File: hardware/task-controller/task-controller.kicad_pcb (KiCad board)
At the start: 2 copper layers, 64 parts, among them J1 USB_C_Receptacle_USB2.0_16P, SW1 User, SW2 RST, SW3 BOOTSEL, U1 RP2040, U2 TPS61023DRL, U3 FM24C64B, U4 W25Q32JVSS, U5 XC6206PxxxMR, Y1 12MHz

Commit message: started layout
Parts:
- removed BT1: Conn_01x02, Connector_JST:JST_PH_S2B-PH-SM4-TB_1x02-1MP_P2.00mm_Horizontal
- removed the C20 at (120.8, 67.9)
- removed the C21 at (120.8, 70.9)
- removed C3, C4, C5: 10uF, Capacitor_SMD:C_0805_2012Metric
- removed the D1 at (106.7, 83.2)
- removed D2: SS24, Diode_SMD:D_SMA
- removed F1: Polyfuse, Fuse:Fuse_1206_3216Metric
- removed JP1: ISENSE, Jumper:SolderJumper-2_P1.3mm_Bridged2Bar_RoundedPad1.0x1.5mm
- removed JP2: SolderJumper_2_Bridged, Jumper:SolderJumper-2_P1.3mm_Bridged2Bar_RoundedPad1.0x1.5mm
- removed JP3: Power_Bypass, Jumper:SolderJumper-2_P1.3mm_Bridged2Bar_RoundedPad1.0x1.5mm
- removed L1: 2.7uH, cat:Inductor_0806
- removed the R1 at (82.2, 79.9)
- removed the R4 at (82.2, 84.9)
- removed TP1, TP2: TestPoint, TestPoint:TestPoint_Pad_3.0x3.0mm
- removed the U5 at (166.9, 60.4)
- added C1: 1uF, Capacitor_SMD:C_0805_2012Metric, F.Cu at (33.6, 69.9)
- added C23: 1uF, Capacitor_SMD:C_0805_2012Metric, F.Cu at (18.5, 90.4)
- added C8: 1uF, Capacitor_SMD:C_0805_2012Metric, F.Cu at (33.6, 72.9)
- added J2: RGB 1, Connector_JST:JST_PH_B3B-PH-SM4-TB_1x03-1MP_P2.00mm_Vertical, F.Cu at (202.6, 87.2)
- added J3: RGB 2, Connector_JST:JST_PH_B3B-PH-SM4-TB_1x03-1MP_P2.00mm_Vertical, F.Cu at (202.6, 98.5)
- added J4: RGB 3, Connector_JST:JST_PH_B3B-PH-SM4-TB_1x03-1MP_P2.00mm_Vertical, F.Cu at (202.6, 109.8)
- added J5: Micro_SD_Card, Connector_Card:microSD_HC_Hirose_DM3AT-SF-PEJM5, F.Cu at (137.6, 84.3)
- added J6: Conn_01x06, Connector_PinHeader_2.54mm:PinHeader_1x06_P2.54mm_Vertical, F.Cu at (29.0, 70.7)
- added R23: 5.1k, Resistor_SMD:R_0402_1005Metric, F.Cu at (91.3, 16.8)
- added R24: 10k, Resistor_SMD:R_0402_1005Metric, F.Cu at (74.1, 0.49)
- added R25: 10k, Resistor_SMD:R_0402_1005Metric, F.Cu at (74.1, 2.48)
- added R26: 10k, Resistor_SMD:R_0402_1005Metric, F.Cu at (74.1, 4.47)
- added R27: 10k, Resistor_SMD:R_0402_1005Metric, F.Cu at (74.1, 6.46)
- added R28: 10k, Resistor_SMD:R_0402_1005Metric, F.Cu at (74.1, 8.46)
- added R29: 10k, Resistor_SMD:R_0402_1005Metric, F.Cu at (74.1, 10.4)
- added R30: 10k, Resistor_SMD:R_0402_1005Metric, F.Cu at (74.1, 12.4)
- added R31: 1k, Resistor_SMD:R_0402_1005Metric, F.Cu at (17.7, 69.3)
- added R32: 5.1k, Resistor_SMD:R_0402_1005Metric, F.Cu at (17.7, 71.3)
- added R33: 5.1k, Resistor_SMD:R_0402_1005Metric, F.Cu at (17.7, 73.3)
- added R34: 5.1k, Resistor_SMD:R_0402_1005Metric, F.Cu at (17.7, 75.3)
- added R35: 5.1k, Resistor_SMD:R_0402_1005Metric, F.Cu at (17.7, 77.3)
- added R36: 5.1k, Resistor_SMD:R_0402_1005Metric, F.Cu at (17.7, 79.3)
- added R37: 5.1k, Resistor_SMD:R_0402_1005Metric, F.Cu at (17.7, 81.3)
- added R38: 5.1k, Resistor_SMD:R_0402_1005Metric, F.Cu at (91.3, 18.8)
- added SW10: MATRIX, Connector_JST:JST_PH_B2B-PH-SM4-TB_1x02-1MP_P2.00mm_Vertical, F.Cu at (249.0, 86.6)
- added SW11: MATRIX, Connector_JST:JST_PH_B2B-PH-SM4-TB_1x02-1MP_P2.00mm_Vertical, F.Cu at (260.0, 86.6)
- added SW12: MATRIX, Connector_JST:JST_PH_B2B-PH-SM4-TB_1x02-1MP_P2.00mm_Vertical, F.Cu at (271.0, 86.6)
- added SW13: MATRIX, Connector_JST:JST_PH_B2B-PH-SM4-TB_1x02-1MP_P2.00mm_Vertical, F.Cu at (216.0, 98.2)
- added SW14: MATRIX, Connector_JST:JST_PH_B2B-PH-SM4-TB_1x02-1MP_P2.00mm_Vertical, F.Cu at (227.0, 98.2)
- added SW15: MATRIX, Connector_JST:JST_PH_B2B-PH-SM4-TB_1x02-1MP_P2.00mm_Vertical, F.Cu at (238.0, 98.2)
- added SW16: MATRIX, Connector_JST:JST_PH_B2B-PH-SM4-TB_1x02-1MP_P2.00mm_Vertical, F.Cu at (249.0, 98.2)
- added SW17: MATRIX, Connector_JST:JST_PH_B2B-PH-SM4-TB_1x02-1MP_P2.00mm_Vertical, F.Cu at (260.0, 98.2)
- added SW18: MATRIX, Connector_JST:JST_PH_B2B-PH-SM4-TB_1x02-1MP_P2.00mm_Vertical, F.Cu at (271.0, 98.2)
- added SW19: MATRIX, Connector_JST:JST_PH_B2B-PH-SM4-TB_1x02-1MP_P2.00mm_Vertical, F.Cu at (216.0, 109.8)
- added SW2: MATRIX, Connector_JST:JST_PH_B2B-PH-SM4-TB_1x02-1MP_P2.00mm_Vertical, F.Cu at (227.0, 75.0)
- added SW20: MATRIX, Connector_JST:JST_PH_B2B-PH-SM4-TB_1x02-1MP_P2.00mm_Vertical, F.Cu at (227.0, 109.8)
- added SW21: MATRIX, Connector_JST:JST_PH_B2B-PH-SM4-TB_1x02-1MP_P2.00mm_Vertical, F.Cu at (238.0, 109.8)
- added SW22: MATRIX, Connector_JST:JST_PH_B2B-PH-SM4-TB_1x02-1MP_P2.00mm_Vertical, F.Cu at (249.0, 109.8)
- added SW23: MATRIX, Connector_JST:JST_PH_B2B-PH-SM4-TB_1x02-1MP_P2.00mm_Vertical, F.Cu at (260.0, 109.8)
- added SW24: MATRIX, Connector_JST:JST_PH_B2B-PH-SM4-TB_1x02-1MP_P2.00mm_Vertical, F.Cu at (271.0, 109.8)
- added SW25: MATRIX, Connector_JST:JST_PH_B2B-PH-SM4-TB_1x02-1MP_P2.00mm_Vertical, F.Cu at (216.0, 121.4)
- added SW26: MATRIX, Connector_JST:JST_PH_B2B-PH-SM4-TB_1x02-1MP_P2.00mm_Vertical, F.Cu at (227.0, 121.4)
- added SW27: MATRIX, Connector_JST:JST_PH_B2B-PH-SM4-TB_1x02-1MP_P2.00mm_Vertical, F.Cu at (238.0, 121.4)
- added SW28: MATRIX, Connector_JST:JST_PH_B2B-PH-SM4-TB_1x02-1MP_P2.00mm_Vertical, F.Cu at (249.0, 121.4)
- added SW29: MATRIX, Connector_JST:JST_PH_B2B-PH-SM4-TB_1x02-1MP_P2.00mm_Vertical, F.Cu at (260.0, 121.4)
- added SW3: MATRIX, Connector_JST:JST_PH_B2B-PH-SM4-TB_1x02-1MP_P2.00mm_Vertical, F.Cu at (238.0, 75.0)
- added SW30: MATRIX, Connector_JST:JST_PH_B2B-PH-SM4-TB_1x02-1MP_P2.00mm_Vertical, F.Cu at (271.0, 121.4)
- added SW31: MATRIX, Connector_JST:JST_PH_B2B-PH-SM4-TB_1x02-1MP_P2.00mm_Vertical, F.Cu at (216.0, 133.0)
- added SW32: MATRIX, Connector_JST:JST_PH_B2B-PH-SM4-TB_1x02-1MP_P2.00mm_Vertical, F.Cu at (227.0, 133.0)
- added SW33: MATRIX, Connector_JST:JST_PH_B2B-PH-SM4-TB_1x02-1MP_P2.00mm_Vertical, F.Cu at (238.0, 133.0)
- added SW34: MATRIX, Connector_JST:JST_PH_B2B-PH-SM4-TB_1x02-1MP_P2.00mm_Vertical, F.Cu at (249.0, 133.0)
- added SW35: MATRIX, Connector_JST:JST_PH_B2B-PH-SM4-TB_1x02-1MP_P2.00mm_Vertical, F.Cu at (260.0, 133.0)
- added SW36: MATRIX, Connector_JST:JST_PH_B2B-PH-SM4-TB_1x02-1MP_P2.00mm_Vertical, F.Cu at (271.0, 133.0)
- added SW37: MATRIX, Connector_JST:JST_PH_B2B-PH-SM4-TB_1x02-1MP_P2.00mm_Vertical, F.Cu at (216.0, 144.6)
- added SW38: MATRIX, Connector_JST:JST_PH_B2B-PH-SM4-TB_1x02-1MP_P2.00mm_Vertical, F.Cu at (227.0, 144.6)
- added SW39: MATRIX, Connector_JST:JST_PH_B2B-PH-SM4-TB_1x02-1MP_P2.00mm_Vertical, F.Cu at (238.0, 144.6)
- added SW4: MATRIX, Connector_JST:JST_PH_B2B-PH-SM4-TB_1x02-1MP_P2.00mm_Vertical, F.Cu at (249.0, 75.0)
- added SW40: MATRIX, Connector_JST:JST_PH_B2B-PH-SM4-TB_1x02-1MP_P2.00mm_Vertical, F.Cu at (249.0, 144.6)
- added SW41: MATRIX, Connector_JST:JST_PH_B2B-PH-SM4-TB_1x02-1MP_P2.00mm_Vertical, F.Cu at (260.0, 144.6)
- added SW42: MATRIX, Connector_JST:JST_PH_B2B-PH-SM4-TB_1x02-1MP_P2.00mm_Vertical, F.Cu at (271.0, 144.6)
- added SW43: MATRIX, Connector_JST:JST_PH_B2B-PH-SM4-TB_1x02-1MP_P2.00mm_Vertical, F.Cu at (216.0, 156.2)
- added SW44: MATRIX, Connector_JST:JST_PH_B2B-PH-SM4-TB_1x02-1MP_P2.00mm_Vertical, F.Cu at (227.0, 156.2)
- added SW45: MATRIX, Connector_JST:JST_PH_B2B-PH-SM4-TB_1x02-1MP_P2.00mm_Vertical, F.Cu at (238.0, 156.2)
- added SW46: MATRIX, Connector_JST:JST_PH_B2B-PH-SM4-TB_1x02-1MP_P2.00mm_Vertical, F.Cu at (249.0, 156.2)
- added SW47: MATRIX, Connector_JST:JST_PH_B2B-PH-SM4-TB_1x02-1MP_P2.00mm_Vertical, F.Cu at (260.0, 156.2)
- added SW48: MATRIX, Connector_JST:JST_PH_B2B-PH-SM4-TB_1x02-1MP_P2.00mm_Vertical, F.Cu at (271.0, 156.2)
- added SW49: MATRIX, Connector_JST:JST_PH_B2B-PH-SM4-TB_1x02-1MP_P2.00mm_Vertical, F.Cu at (203.0, 75.5)
- added SW5: MATRIX, Connector_JST:JST_PH_B2B-PH-SM4-TB_1x02-1MP_P2.00mm_Vertical, F.Cu at (260.0, 75.0)
- added SW52: User, cat:TS-1088-AR02016, F.Cu at (93.7, 22.1)
- added SW6: MATRIX, Connector_JST:JST_PH_B2B-PH-SM4-TB_1x02-1MP_P2.00mm_Vertical, F.Cu at (271.0, 75.0)
- added SW7: MATRIX, Connector_JST:JST_PH_B2B-PH-SM4-TB_1x02-1MP_P2.00mm_Vertical, F.Cu at (216.0, 86.6)
- added SW8: MATRIX, Connector_JST:JST_PH_B2B-PH-SM4-TB_1x02-1MP_P2.00mm_Vertical, F.Cu at (227.0, 86.6)
- added SW9: MATRIX, Connector_JST:JST_PH_B2B-PH-SM4-TB_1x02-1MP_P2.00mm_Vertical, F.Cu at (238.0, 86.6)
- added U1: XC6206PxxxMR, Package_TO_SOT_SMD:SOT-23-3, F.Cu at (33.9, 76.8)
- added U6: PCF8523T, Package_SO:SOIC-8_3.9x4.9mm_P1.27mm, F.Cu at (20.5, 85.6)
- C10: renamed from C6; footprint Capacitor_SMD:C_0603_1608Metric -> Capacitor_SMD:C_0402_1005Metric
- C11: renamed from C7; footprint Capacitor_SMD:C_0603_1608Metric -> Capacitor_SMD:C_0402_1005Metric
- C12: renamed from C2; footprint Capacitor_SMD:C_0603_1608Metric -> Capacitor_SMD:C_0402_1005Metric
- C13: renamed from C8; footprint Capacitor_SMD:C_0603_1608Metric -> Capacitor_SMD:C_0402_1005Metric
- C14: renamed from C9; footprint Capacitor_SMD:C_0603_1608Metric -> Capacitor_SMD:C_0402_1005Metric
- C15: renamed from C10; footprint Capacitor_SMD:C_0603_1608Metric -> Capacitor_SMD:C_0402_1005Metric
- C16: renamed from C11; footprint Capacitor_SMD:C_0603_1608Metric -> Capacitor_SMD:C_0402_1005Metric
- C17: renamed from C12; footprint Capacitor_SMD:C_0603_1608Metric -> Capacitor_SMD:C_0402_1005Metric
- C18: renamed from C13; footprint Capacitor_SMD:C_0603_1608Metric -> Capacitor_SMD:C_0402_1005Metric
- C19: renamed from C14; footprint Capacitor_SMD:C_0603_1608Metric -> Capacitor_SMD:C_0402_1005Metric
- C21: renamed from C19; footprint Capacitor_SMD:C_0603_1608Metric -> Capacitor_SMD:C_0402_1005Metric
- C7: renamed from C1; footprint Capacitor_SMD:C_0603_1608Metric -> Capacitor_SMD:C_0402_1005Metric
- R1: renamed from R21; footprint Resistor_SMD:R_0603_1608Metric -> Resistor_SMD:R_0402_1005Metric
- R11: renamed from R2; footprint Resistor_SMD:R_0603_1608Metric -> Resistor_SMD:R_0402_1005Metric
- R12: renamed from R3; footprint Connector_JST:JST_XH_B2B-XH-AM_1x02_P2.50mm_Vertical -> Connector_JST:JST_PH_B2B-PH-K_1x02_P2.00mm_Vertical
- R14: renamed from R12; footprint Resistor_SMD:R_0603_1608Metric -> Resistor_SMD:R_0402_1005Metric
- R15: renamed from R14; footprint Resistor_SMD:R_0603_1608Metric -> Resistor_SMD:R_0402_1005Metric
- R16: renamed from R17; footprint Resistor_SMD:R_0603_1608Metric -> Resistor_SMD:R_0402_1005Metric
- R18: renamed from R16; footprint Resistor_SMD:R_0603_1608Metric -> Resistor_SMD:R_0402_1005Metric
- R19: renamed from R15; footprint Resistor_SMD:R_0603_1608Metric -> Resistor_SMD:R_0402_1005Metric
- R2: renamed from R8; footprint Resistor_SMD:R_0603_1608Metric -> Resistor_SMD:R_0402_1005Metric
- R20: renamed from R19; footprint Resistor_SMD:R_0603_1608Metric -> Resistor_SMD:R_0402_1005Metric
- R21: renamed from R20; footprint Resistor_SMD:R_0603_1608Metric -> Resistor_SMD:R_0402_1005Metric
- R22: renamed from R18; footprint Resistor_SMD:R_0603_1608Metric -> Resistor_SMD:R_0402_1005Metric
- R3: renamed from R22; footprint Resistor_SMD:R_0603_1608Metric -> Resistor_SMD:R_0402_1005Metric
- R5: value 100k -> 10k; footprint Resistor_SMD:R_0603_1608Metric -> Resistor_SMD:R_0402_1005Metric
- R6: value 470k -> 5.1k; footprint Resistor_SMD:R_0603_1608Metric -> Resistor_SMD:R_0402_1005Metric
- R7: value 100k -> 5.1k; footprint Resistor_SMD:R_0603_1608Metric -> Resistor_SMD:R_0402_1005Metric
- R9: renamed from R11; footprint Resistor_SMD:R_0603_1608Metric -> Resistor_SMD:R_0402_1005Metric
- SW1: value User -> MATRIX; footprint cat:TS-1088-AR02016 -> Connector_JST:JST_PH_B2B-PH-SM4-TB_1x02-1MP_P2.00mm_Vertical
- U2: value TPS61023DRL -> 74125; footprint Package_TO_SOT_SMD:SOT-563 -> Package_SO:SOIC-14_3.9x8.7mm_P1.27mm
- moved SW1 120.0 mm to (216.0, 75.0)
- moved R5 105.5 mm to (91.3, 10.9)
- moved C13 95.6 mm to (173.6, 83.4), turned to 180 degrees
- moved C14 95.5 mm to (173.4, 87.8), turned to 180 degrees
- moved U2 94.0 mm to (94.0, 4.76)
- moved R6 89.6 mm to (91.3, 12.8), turned to 0 degrees
- moved C15 89.3 mm to (167.2, 90.2), turned to 90 degrees
- moved R7 87.2 mm to (91.3, 14.8), turned to 0 degrees
- moved C18 86.0 mm to (167.6, 78.0), turned to -90 degrees
- moved C19 84.8 mm to (164.6, 90.2), turned to 90 degrees
- moved C17 83.5 mm to (161.6, 83.4)
- moved C16 83.2 mm to (161.4, 87.0)
- moved C20 54.4 mm to (161.6, 90.0)
- moved C9 53.7 mm to (161.6, 92.4)
- moved SW50 46.1 mm to (72.4, 117.0), turned to 90 degrees
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- renumbered C15 to C2, C18 to C20, C16 to C6, C17 to C9, D3 to D1, R13 to R10, R10 to R4, R9 to R8, SW3 to SW50, SW2 to SW51, U4 to U3, U1 to U4, U3 to U5
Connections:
- net /BATTERY_SENSE renamed /BRIGHTNESS_POT
- C13 pad 2: VDD -> +3V3
- C14 pad 2: VDD -> +3V3
- C15 pad 2: VDD -> +3V3
- C16 pad 2: VDD -> +3V3
- C17 pad 2: VDD -> +3V3
- C18 pad 2: VDD -> +3V3
- C19 pad 2: VDD -> +3V3
- C20 pad 2: VDD -> +3V3
- C21 pad 1: VDD -> +3V3
- C7 pad 2: VDD -> +3V3
- J1 pad A4: VBUS -> +5V
- J1 pad A9: VBUS -> +5V
- J1 pad B4: VBUS -> +5V
- J1 pad B9: VBUS -> +5V
- R10 pad 1: Net-(U1-GPIO8) -> Net-(U4-GPIO4)
- R11 pad 1: VDD -> +3V3
- R20 pad 2: VDD -> +3V3
- R21 pad 2: VDD -> +3V3
- R22 pad 1: VDD -> GND
- R3 pad 1: VDD -> +3V3
- R5 pad 1: /Power/Battery_Sense -> unconnected-(R5-Pad1)
- R5 pad 2: Net-(JP2-B) -> unconnected-(R5-Pad2)
- R6 pad 1: /Power/4V_REG -> Net-(U2B-EN)
- R6 pad 2: Net-(U2-FB) -> GND
- R7 pad 1: Net-(U2-FB) -> Net-(U2C-EN)
- R9 pad 2: VDD -> +3V3
- SW1 pad 1: /BUTTON -> /Button Matrix/R1
- SW1 pad 2: GND -> /Button Matrix/C1
- U2 pad 1: Net-(U2-FB) -> Net-(U2A-EN)
- U2 pad 2: +BATT -> /RGB_1
- U2 pad 3: +BATT -> /User Interface/RGB_1_BUF
- U2 pad 4: GND -> Net-(U2B-EN)
- U2 pad 5: Net-(U2-SW) -> /RGB_2
- U2 pad 6: /Power/4V_REG -> /User Interface/RGB_2_BUF
- U3 pad 8: VDD -> +3V3
- U4 pad 1: VDD -> +3V3
- U4 pad 10: VDD -> +3V3
- U4 pad 11: Net-(U1-GPIO8) -> /Button Matrix/R1
- U4 pad 12: unconnected-(U1-GPIO9-Pad12) -> /Button Matrix/R2
- U4 pad 13: unconnected-(U1-GPIO10-Pad13) -> /Button Matrix/R3
- U4 pad 14: unconnected-(U1-GPIO11-Pad14) -> /Button Matrix/R4
- U4 pad 15: unconnected-(U1-GPIO12-Pad15) -> /Button Matrix/R5
- U4 pad 16: unconnected-(U1-GPIO13-Pad16) -> /Button Matrix/R6
- U4 pad 17: unconnected-(U1-GPIO14-Pad17) -> /Button Matrix/R7
- U4 pad 18: unconnected-(U1-GPIO15-Pad18) -> /Button Matrix/C1
- U4 pad 2: Net-(U1-GPIO0) -> /UART_TX
- U4 pad 22: VDD -> +3V3
- U4 pad 27: unconnected-(U1-GPIO16-Pad27) -> /Button Matrix/C2
- U4 pad 28: unconnected-(U1-GPIO17-Pad28) -> /Button Matrix/C3
- U4 pad 29: unconnected-(U1-GPIO18-Pad29) -> /SPI_SCK
- U4 pad 3: Net-(U1-GPIO1) -> /UART_RX
- U4 pad 30: unconnected-(U1-GPIO19-Pad30) -> /SPI_MOSI
- U4 pad 31: unconnected-(U1-GPIO20-Pad31) -> /SPI_MISO
- U4 pad 32: unconnected-(U1-GPIO21-Pad32) -> /Button Matrix/C4
- U4 pad 33: VDD -> +3V3
- U4 pad 34: unconnected-(U1-GPIO22-Pad34) -> /Button Matrix/C5
- U4 pad 35: unconnected-(U1-GPIO23-Pad35) -> /Button Matrix/C6
- U4 pad 36: unconnected-(U1-GPIO24-Pad36) -> /Button Matrix/C7
- U4 pad 37: unconnected-(U1-GPIO25-Pad37) -> /SD_CS
- U4 pad 40: unconnected-(U1-GPIO28_ADC2-Pad40) -> /RTC_INT
- U4 pad 41: unconnected-(U1-GPIO29_ADC3-Pad41) -> /BUTTON
- U4 pad 42: VDD -> +3V3
- U4 pad 43: VDD -> +3V3
- U4 pad 44: VDD -> +3V3
- U4 pad 48: VDD -> +3V3
- U4 pad 49: VDD -> +3V3
- U4 pad 6: /EEPROM_WP -> Net-(U4-GPIO4)
- U4 pad 7: unconnected-(U1-GPIO5-Pad7) -> /RGB_1
- U4 pad 8: unconnected-(U1-GPIO6-Pad8) -> /RGB_2
- U4 pad 9: /BUTTON -> /RGB_3
- U5 pad 8: VDD -> +3V3
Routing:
- net Net-(U2-SW): track 3.27 -> 0.00 mm
- removed copper zone on F.Cu, net +BATT
- removed copper zone on F.Cu, net /Power/4V_REG
- removed copper zone on F.Cu, net GND
- removed copper zone on F.Cu, net Net-(U2-FB)
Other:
- board outline added: 150 x 100 mm
- board text removed: "Boost Converter 4V out"

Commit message: mostly done layout
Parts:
- added C24: 0.1uF, Capacitor_SMD:C_0402_1005Metric, F.Cu at (148.2, 84.2)
- moved R24 176.5 mm to (205.1, 118.8)
- moved R25 176.5 mm to (205.1, 120.8)
- moved R26 176.5 mm to (205.1, 122.8)
- moved R27 176.5 mm to (205.1, 124.8)
- moved R28 176.5 mm to (205.1, 126.8)
- moved R29 176.5 mm to (205.1, 128.8)
- moved R30 176.5 mm to (205.1, 130.8)
- moved J6 155.7 mm to (184.6, 64.6), turned to 90 degrees
- moved U2 143.3 mm to (189.1, 112.0)
- moved R35 134.3 mm to (152.0, 81.0), turned to 90 degrees
- moved R33 133.2 mm to (150.0, 88.4), turned to -90 degrees
- moved R34 132.2 mm to (149.6, 84.0), turned to 90 degrees
- moved R37 131.1 mm to (148.8, 78.8)
- moved R32 130.8 mm to (147.4, 88.4), turned to -90 degrees
- moved R36 130.7 mm to (148.4, 81.0), turned to -90 degrees
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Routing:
- net +3V3: track 0.00 -> 9.53 mm, vias 0 -> 3
- net GND: track 0.00 -> 2.44 mm, vias 0 -> 2
- added copper zone on In2.Cu, net +3V3
- added copper zone on In1.Cu, net GND
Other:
- copper layers 2 -> 4

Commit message: started routing
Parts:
- moved U2 33.1 mm to (189.7, 78.9), turned to -90 degrees
- moved D1 21.1 mm to (182.0, 55.6)
- moved R10 21.1 mm to (178.2, 55.6)
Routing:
- net /Button Matrix/R6: track 0.00 -> 112.3 mm, vias 0 -> 2
- net /Button Matrix/R5: track 0.00 -> 95.4 mm, vias 0 -> 2
- net /Button Matrix/R4: track 0.00 -> 82.0 mm, vias 0 -> 2
- net /Button Matrix/R3: track 0.00 -> 74.1 mm, vias 0 -> 2
- net /Button Matrix/R2: track 0.00 -> 58.0 mm, vias 0 -> 2
- net /USB_D+: track 0.00 -> 52.6 mm
- net /USB_D-: track 0.00 -> 52.3 mm
- net GND: track 2.44 -> 54.0 mm, vias 2 -> 32
- net /Button Matrix/C1: track 0.00 -> 49.1 mm
- net /Button Matrix/R1: track 0.00 -> 45.4 mm, vias 0 -> 2
- net /SCL: track 0.00 -> 37.0 mm, vias 0 -> 2
- net /Button Matrix/R7: track 0.00 -> 36.3 mm, vias 0 -> 2
- net +3V3: track 9.53 -> 45.5 mm, vias 3 -> 20
- net /SDA: track 0.00 -> 35.8 mm, vias 0 -> 2
- net /SPI_MISO: track 0.00 -> 32.2 mm, vias 0 -> 2
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- added copper zone on B.Cu, net +5V

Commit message: stuff
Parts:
- added C19: 0.1uF, Capacitor_SMD:C_0402_1005Metric, F.Cu at (193.5, 84.4)
- moved R7 122.0 mm to (191.1, 85.0), turned to 180 degrees
- moved R23 119.9 mm to (195.2, 76.6), turned to -90 degrees
- moved R6 111.2 mm to (183.8, 74.6), turned to 180 degrees
- moved D1 45.7 mm to (159.4, 95.3), turned to 90 degrees
- moved R10 40.5 mm to (159.4, 91.5), turned to -90 degrees
- moved J2 26.8 mm to (192.2, 111.9)
- moved J3 26.8 mm to (192.2, 123.2)
- moved J4 26.8 mm to (192.2, 134.4)
- moved R21 8.00 mm to (180.8, 95.7), turned to -90 degrees
- moved R20 7.54 mm to (178.4, 95.7), turned to -90 degrees
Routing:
- net Net-(U4-GPIO4): track 0.00 -> 27.0 mm, vias 0 -> 2
- net /RGB_1: track 0.00 -> 17.7 mm, vias 0 -> 2
- net /RGB_3: track 0.00 -> 13.4 mm
- net /RGB_2: track 0.00 -> 13.3 mm, vias 0 -> 2
- net Net-(U2B-EN): track 0.00 -> 6.67 mm
- net Net-(U2C-EN): track 0.00 -> 5.45 mm
- net GND: track 54.0 -> 59.2 mm, vias 32 -> 34
- net +3V3: track 45.5 -> 49.5 mm, vias 20 -> 23
- net Net-(U2A-EN): track 0.00 -> 3.96 mm
- net /SCL: track 37.0 -> 40.5 mm, vias 2 -> 3
- net +5V: track 8.24 -> 11.6 mm, vias 3 -> 4
- net /SDA: track 35.8 -> 38.4 mm, vias 2 -> 3
- net /UART_TX: track 26.0 -> 26.6 mm, vias 1 -> 2
- net /UART_RX: track 24.4 -> 24.7 mm, vias 1 -> 2

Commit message: changed board size
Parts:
- removed the C19 at (170.0, 83.8)
- removed R5: 10k, Resistor_SMD:R_0402_1005Metric
- added BT1: Battery_Cell, cat:XDCR-1220-006, F.Cu at (55.5, 69.5)
- added C22: 10uF, Capacitor_SMD:C_0603_1608Metric, F.Cu at (45.9, 53.2)
- added C25: 10uF, Capacitor_SMD:C_0603_1608Metric, F.Cu at (9.76, 77.8)
- added C26: 10uF, Capacitor_SMD:C_0603_1608Metric, F.Cu at (24.0, 78.0)
- added C27: 10uF, Capacitor_SMD:C_0603_1608Metric, F.Cu at (38.5, 78.0)
- added C3: 100uF, Capacitor_SMD:C_Elec_6.3x7.7, F.Cu at (9.50, 83.0)
- added C4: 100uF, Capacitor_SMD:C_Elec_6.3x7.7, F.Cu at (23.5, 83.0)
- added C5: 100uF, Capacitor_SMD:C_Elec_6.3x7.7, F.Cu at (38.2, 83.0)
- added H1: MountingHole_Pad, MountingHole:MountingHole_2.7mm_M2.5_Pad_TopBottom, F.Cu at (3.00, 3.00)
- added H2: MountingHole_Pad, MountingHole:MountingHole_2.7mm_M2.5_Pad_TopBottom, F.Cu at (65.0, 3.00)
- added H3: MountingHole_Pad, MountingHole:MountingHole_2.7mm_M2.5_Pad_TopBottom, F.Cu at (137.0, 3.00)
- added H4: MountingHole_Pad, MountingHole:MountingHole_2.7mm_M2.5_Pad_TopBottom, F.Cu at (3.00, 97.0)
- added H5: MountingHole_Pad, MountingHole:MountingHole_2.7mm_M2.5_Pad_TopBottom, F.Cu at (65.0, 97.0)
- added H6: MountingHole_Pad, MountingHole:MountingHole_2.7mm_M2.5_Pad_TopBottom, F.Cu at (137.0, 97.0)
- added J7: Conn_01x02, Connector_PinHeader_2.54mm:PinHeader_1x02_P2.54mm_Vertical, F.Cu at (21.5, 50.8)
- added RV1: Brightness, Connector_JST:JST_PH_B3B-PH-SM4-TB_1x03-1MP_P2.00mm_Vertical, F.Cu at (22.6, 60.0)
- added Y2: 32.768kHz, Crystal:Crystal_SMD_3215-2Pin_3.2x1.5mm, F.Cu at (34.6, 54.7)
- R12: footprint Connector_JST:JST_PH_B2B-PH-K_1x02_P2.00mm_Vertical -> Connector_JST:JST_PH_B2B-PH-SM4-TB_1x02-1MP_P2.00mm_Vertical
- moved R24 201.1 mm to (61.0, -21.4)
- moved R25 201.1 mm to (61.0, -19.4)
- moved R26 201.1 mm to (61.0, -17.5)
- moved R27 201.1 mm to (61.0, -15.5)
- moved R28 201.1 mm to (61.0, -13.5)
- moved R29 201.1 mm to (61.0, -11.5)
- moved R30 201.1 mm to (61.0, -9.50)
- moved J2 187.5 mm to (8.89, 72.5)
- moved R38 176.7 mm to (9.24, 39.8)
- moved J3 176.6 mm to (23.0, 72.5)
- moved SW52 175.3 mm to (4.15, 42.4), turned to -90 degrees
- moved J4 166.6 mm to (37.5, 72.5)
- moved SW1 156.0 mm to (73.8, 11.0)
- moved SW10 156.0 mm to (106.8, 22.6)
- moved SW11 156.0 mm to (117.8, 22.6)
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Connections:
- U6 pad 3: unconnected-(U6-VBAT-Pad3) -> Net-(BT1-+)
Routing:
- net /Button Matrix/R6: track 112.3 -> 3.99 mm, vias 2 -> 0
- net /User Interface/RGB_1_BUF: track 0.00 -> 96.6 mm, vias 0 -> 4
- net /User Interface/RGB_2_BUF: track 0.00 -> 83.1 mm, vias 0 -> 4
- net /Button Matrix/R5: track 95.4 -> 22.0 mm, vias 2 -> 0
- net /Button Matrix/R4: track 82.0 -> 20.9 mm, vias 2 -> 0
- net /User Interface/RGB_3_BUF: track 0.00 -> 61.0 mm, vias 0 -> 2
- net /Button Matrix/R3: track 74.1 -> 21.0 mm, vias 2 -> 0
- net /BRIGHTNESS_POT: track 0.00 -> 47.3 mm, vias 0 -> 2
- net /BUTTON: track 0.00 -> 46.6 mm, vias 0 -> 2
- net /Button Matrix/C1: track 49.1 -> 5.68 mm
- net /PHOTORESISTOR: track 0.00 -> 39.5 mm, vias 0 -> 2
- net /RTC_INT: track 0.00 -> 38.9 mm, vias 0 -> 4
- net GND: track 59.2 -> 93.1 mm, vias 34 -> 46
- net /Button Matrix/R7: track 36.3 -> 7.18 mm
- net /Button Matrix/R2: track 58.0 -> 29.2 mm, vias 2 -> 1
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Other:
- board size 150 x 100 mm -> 140 x 100 mm

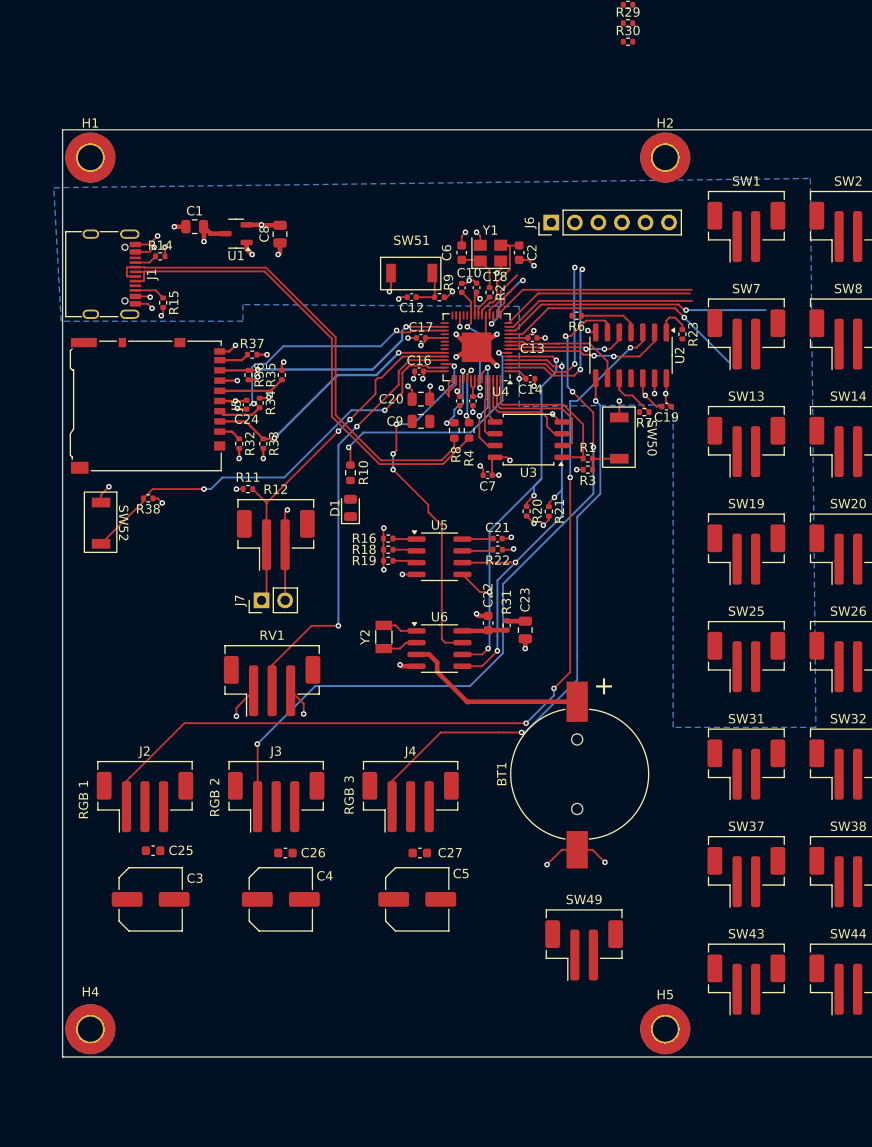
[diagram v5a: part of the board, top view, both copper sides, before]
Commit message: routed RGB section
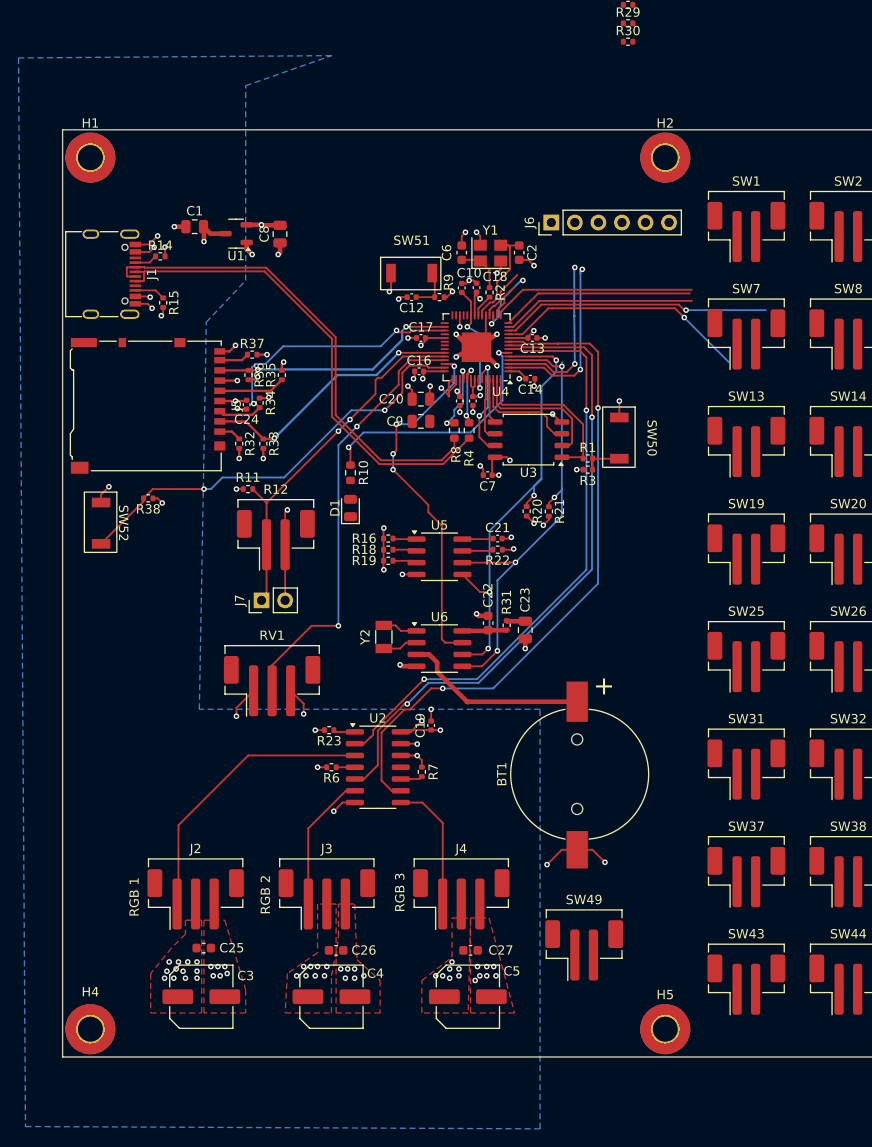
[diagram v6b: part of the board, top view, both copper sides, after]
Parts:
- moved R23 57.2 mm to (28.8, 64.8), turned to 180 degrees
- moved R6 55.4 mm to (29.0, 68.8)
- moved U2 52.1 mm to (34.0, 68.8), turned to 0 degrees
- moved R7 45.6 mm to (38.8, 69.2), turned to 90 degrees
- moved C19 42.7 mm to (39.8, 64.2), turned to 90 degrees
- moved C25 11.8 mm to (15.2, 88.2)
- moved C26 11.8 mm to (29.5, 88.5)
- moved C27 11.8 mm to (44.0, 88.5)
- moved C3 11.8 mm to (15.0, 93.5)
- moved C4 11.8 mm to (29.0, 93.5)
- moved C5 11.8 mm to (43.7, 93.5)
- moved J2 11.8 mm to (14.3, 83.0)
- moved J3 11.8 mm to (28.5, 83.0)
- moved J4 11.8 mm to (43.0, 83.0)
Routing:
- net /User Interface/RGB_2_BUF: track 83.1 -> 14.9 mm, vias 4 -> 0
- net /User Interface/RGB_1_BUF: track 96.6 -> 30.7 mm, vias 4 -> 0
- net /RGB_3: track 13.4 -> 72.8 mm, vias 0 -> 2
- net /RGB_2: track 13.3 -> 70.7 mm
- net /RGB_1: track 17.7 -> 64.7 mm
- net /User Interface/RGB_3_BUF: track 61.0 -> 14.2 mm, vias 2 -> 0
- net Net-(U2B-EN): track 6.67 -> 2.01 mm
- net GND: track 93.1 -> 97.0 mm, vias 46 -> 68
- net +5V: track 11.6 -> 15.4 mm, vias 4 -> 32
- net Net-(U2C-EN): track 5.45 -> 2.38 mm
- net +1V1: track 17.9 -> 15.3 mm
- net Net-(U2A-EN): track 3.96 -> 2.34 mm
- added copper zone on F.Cu, net +5V
- added copper zone on F.Cu, net GND

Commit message: electrical design passes DRC
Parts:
- moved R29 127.1 mm to (137.2, 90.2), turned to -90 degrees
- moved R26 80.1 mm to (68.5, 62.2), turned to 180 degrees
- moved R27 66.0 mm to (62.8, 50.5)
- moved R28 55.5 mm to (66.5, 41.8), turned to 180 degrees
- moved R24 35.9 mm to (67.0, 14.0), turned to 180 degrees
- moved R30 33.7 mm to (66.2, 23.8)
- moved R25 29.6 mm to (67.0, 9.50)
- moved J6 12.5 mm to (42.9, 2.25)
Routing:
- net /Button Matrix/C3: track 0.00 -> 292.0 mm, vias 0 -> 13
- net /Button Matrix/C4: track 0.00 -> 270.9 mm, vias 0 -> 13
- net /Button Matrix/C6: track 0.00 -> 264.7 mm, vias 0 -> 13
- net /Button Matrix/C5: track 0.00 -> 246.2 mm, vias 0 -> 14
- net /Button Matrix/C2: track 0.00 -> 245.2 mm, vias 0 -> 19
- net /Button Matrix/C7: track 0.00 -> 233.4 mm, vias 0 -> 11
- net /Button Matrix/C1: track 5.68 -> 223.5 mm, vias 0 -> 6
- net /Button Matrix/R6: track 3.99 -> 193.5 mm, vias 0 -> 4
- net /Button Matrix/R7: track 7.18 -> 193.2 mm, vias 2 -> 6
- net /Button Matrix/R5: track 22.0 -> 190.1 mm, vias 0 -> 2
- net /Button Matrix/R4: track 20.9 -> 176.1 mm, vias 0 -> 4
- net /Button Matrix/R3: track 21.0 -> 160.8 mm, vias 0 -> 2
- net /Button Matrix/R2: track 29.2 -> 149.1 mm, vias 1 -> 2
- net /Button Matrix/R1: track 27.3 -> 128.6 mm
- net /SPI_SCK: track 7.19 -> 29.1 mm, vias 0 -> 2
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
